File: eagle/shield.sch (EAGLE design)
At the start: 12 parts

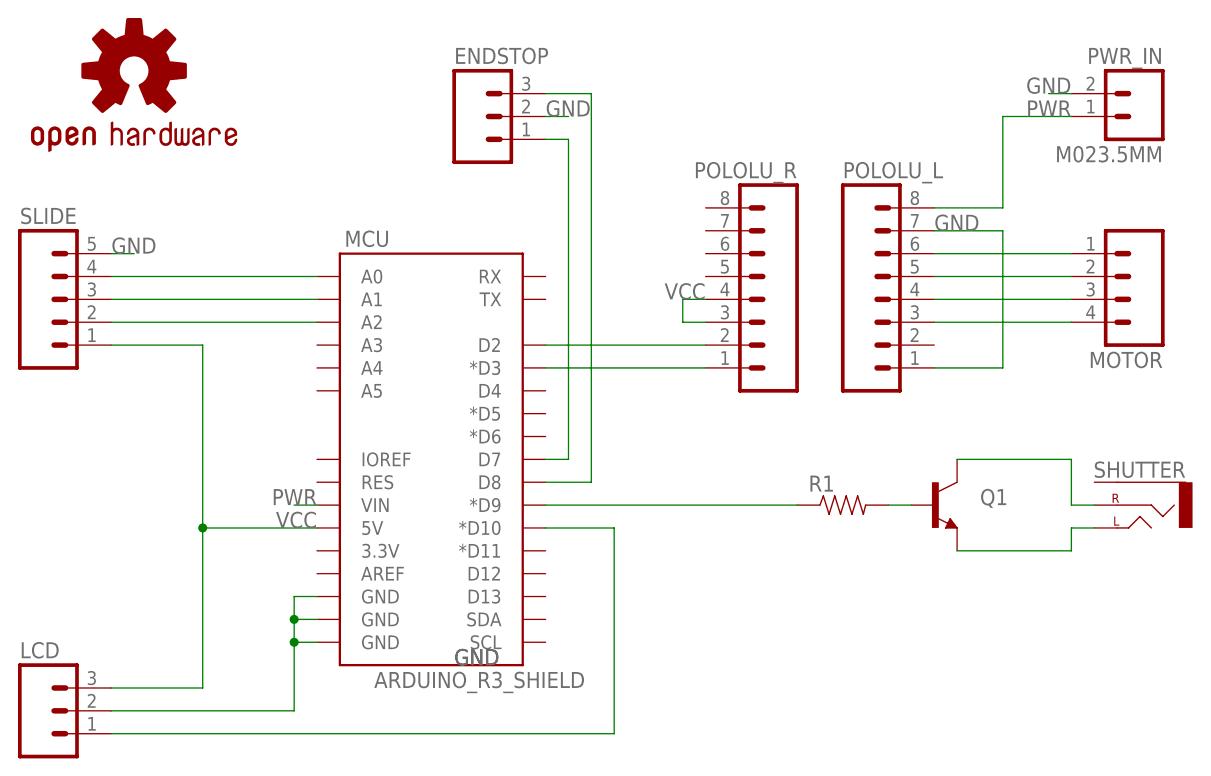
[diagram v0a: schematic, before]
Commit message: updated shield schematics to include a second joystick and two servos to control pan and tilt
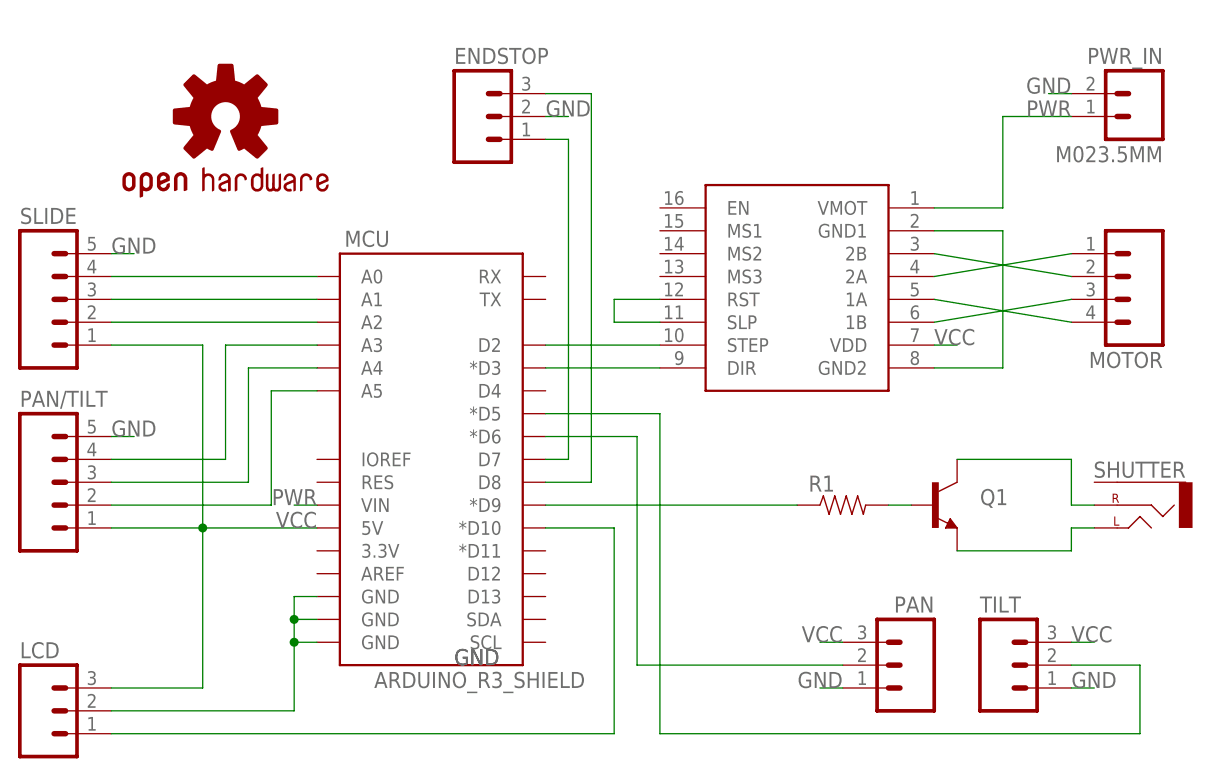
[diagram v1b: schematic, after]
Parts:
- removed POLOLU_L, POLOLU_R: (no value), SparkFun-Connectors:M081X08
- added PAN, TILT: (no value), SparkFun-Connectors:M03PTH
- added PAN/TILT: (no value), SparkFun-Connectors:M05PTH
- added SOCKET: POLOLU DRIVER, reprap:POLOLUESTEPPERDRIVER
- LOGO1: value OSHW-LOGOL -> OSHW-LOGOM; device SparkFun-Aesthetics:OSHW-LOGOL -> SparkFun-Aesthetics:OSHW-LOGOM
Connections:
- removed net N$4: MOTOR.1, POLOLU_L.6
- removed net N$5: MOTOR.2, POLOLU_L.5
- removed net N$6: MOTOR.3, POLOLU_L.4
- removed net N$7: MOTOR.4, POLOLU_L.3
- new net 1A: MOTOR.4, SOCKET.1A
- new net 1B: MOTOR.3, SOCKET.1B
- new net 2A: MOTOR.1, SOCKET.2A
- new net 2B: MOTOR.2, SOCKET.2B
- new net N$15: MCU.*D6, PAN.2
- new net N$18: MCU.*D5, TILT.2
- new net N$19: SOCKET.GND1, SOCKET.GND2
- new net N$20: MCU.A3, PAN/TILT.4
- new net N$21: MCU.A4, PAN/TILT.3
- new net N$22: MCU.A5, PAN/TILT.2
- new net N$23: SOCKET.RST, SOCKET.SLP
- net GND: now also PAN.1, PAN/TILT.5, TILT.1; no longer POLOLU_L.1, POLOLU_L.7
- net N$1: now also SOCKET.STEP; no longer POLOLU_R.2
- net N$2: now also SOCKET.DIR; no longer POLOLU_R.1
- net PWR: now also SOCKET.VMOT; no longer POLOLU_L.8
- net VCC: now also PAN.3, PAN/TILT.1, SOCKET.VDD, TILT.3; no longer POLOLU_R.3, POLOLU_R.4
